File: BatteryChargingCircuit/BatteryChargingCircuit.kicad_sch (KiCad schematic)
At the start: 29 parts, among them J1 USB_B_Micro, U1 TPS61088RHLR, U3 BQ24092DGQR

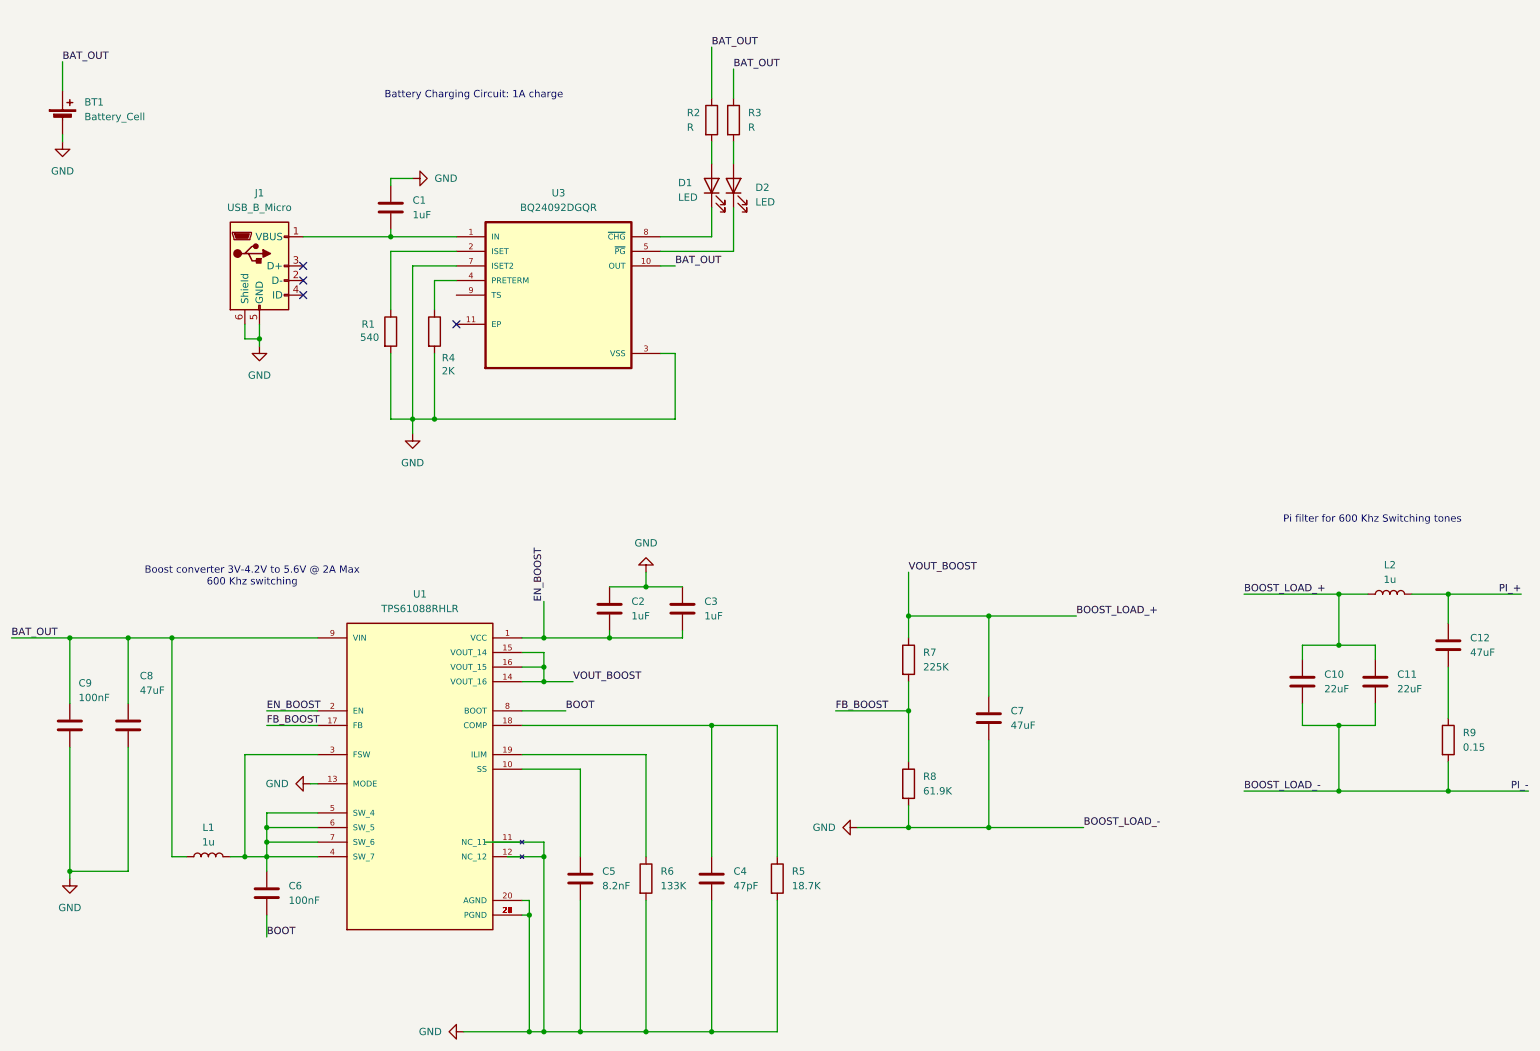
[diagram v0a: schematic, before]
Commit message: fixed mistakes on boost circuit and added LDO circuit
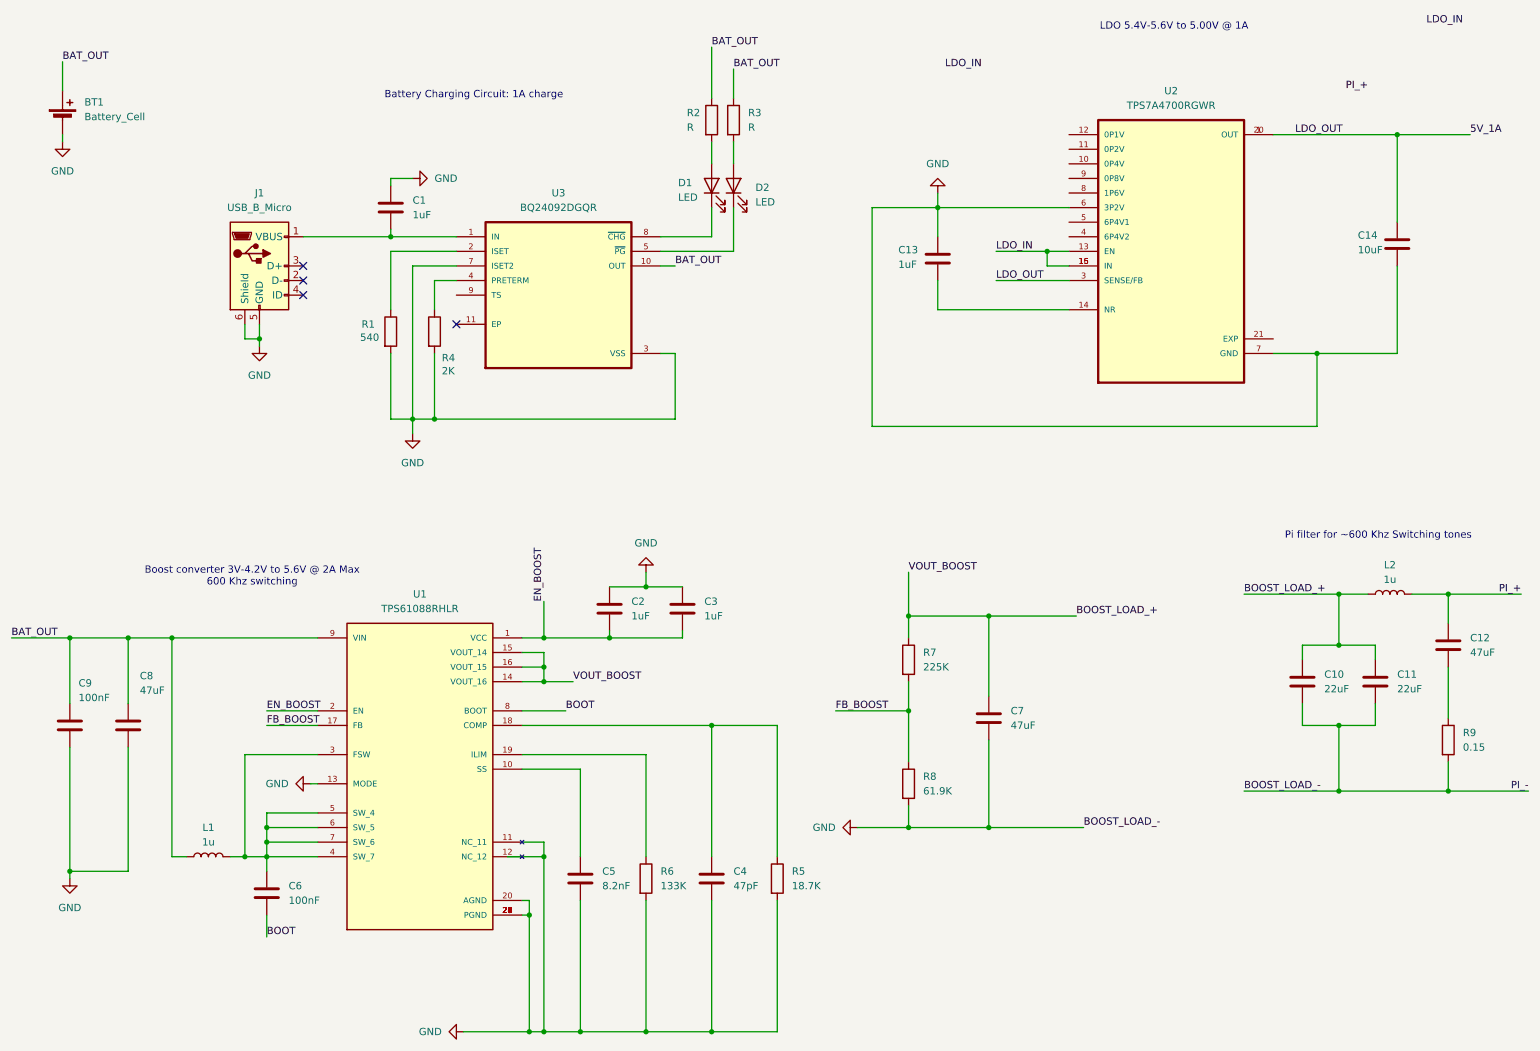
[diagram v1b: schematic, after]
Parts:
- added C13: 1uF, symbol Device:C
- added C14: 10uF, symbol Device:C
- added U2: TPS7A4700RGWR, TPS7A4700RGWR:QFN65P500X500X100-21N, symbol TPS7A4700RGWR:TPS7A4700RGWR
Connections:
- net GND: now also U1.11 (NC_11), C13.1, C14.2, U2.6 (3P2V), U2.7 (GND)
- new net: C13.2, U2.14 (NR)
- new net 5V_1A: C14.1, U2.1 (OUT), U2.20 (OUT), U2.3 (SENSE/FB)
- new net LDO_IN: U2.13 (EN), U2.15 (IN), U2.16 (IN)
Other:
- note added: "LDO 5.4V-5.6V to 5.00V @ 1A"
- note added: "Pi filter for ~600 Khz Switching tones"
- note removed: "Pi filter for 600 Khz Switching tones"
